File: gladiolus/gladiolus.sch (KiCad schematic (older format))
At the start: 143 parts, among them J1 NEIGHBOR1, J2 NEIGHBOR2, J7 BONUS_ROW, Q1 Q_NPN_BEC, U1 THS4520RGT, U2 AD8330ARQZ, U3 AD9283, U4 AD9704, U5 LMH6643, U6 74LVC1G3157, U7 74LVC1G3157

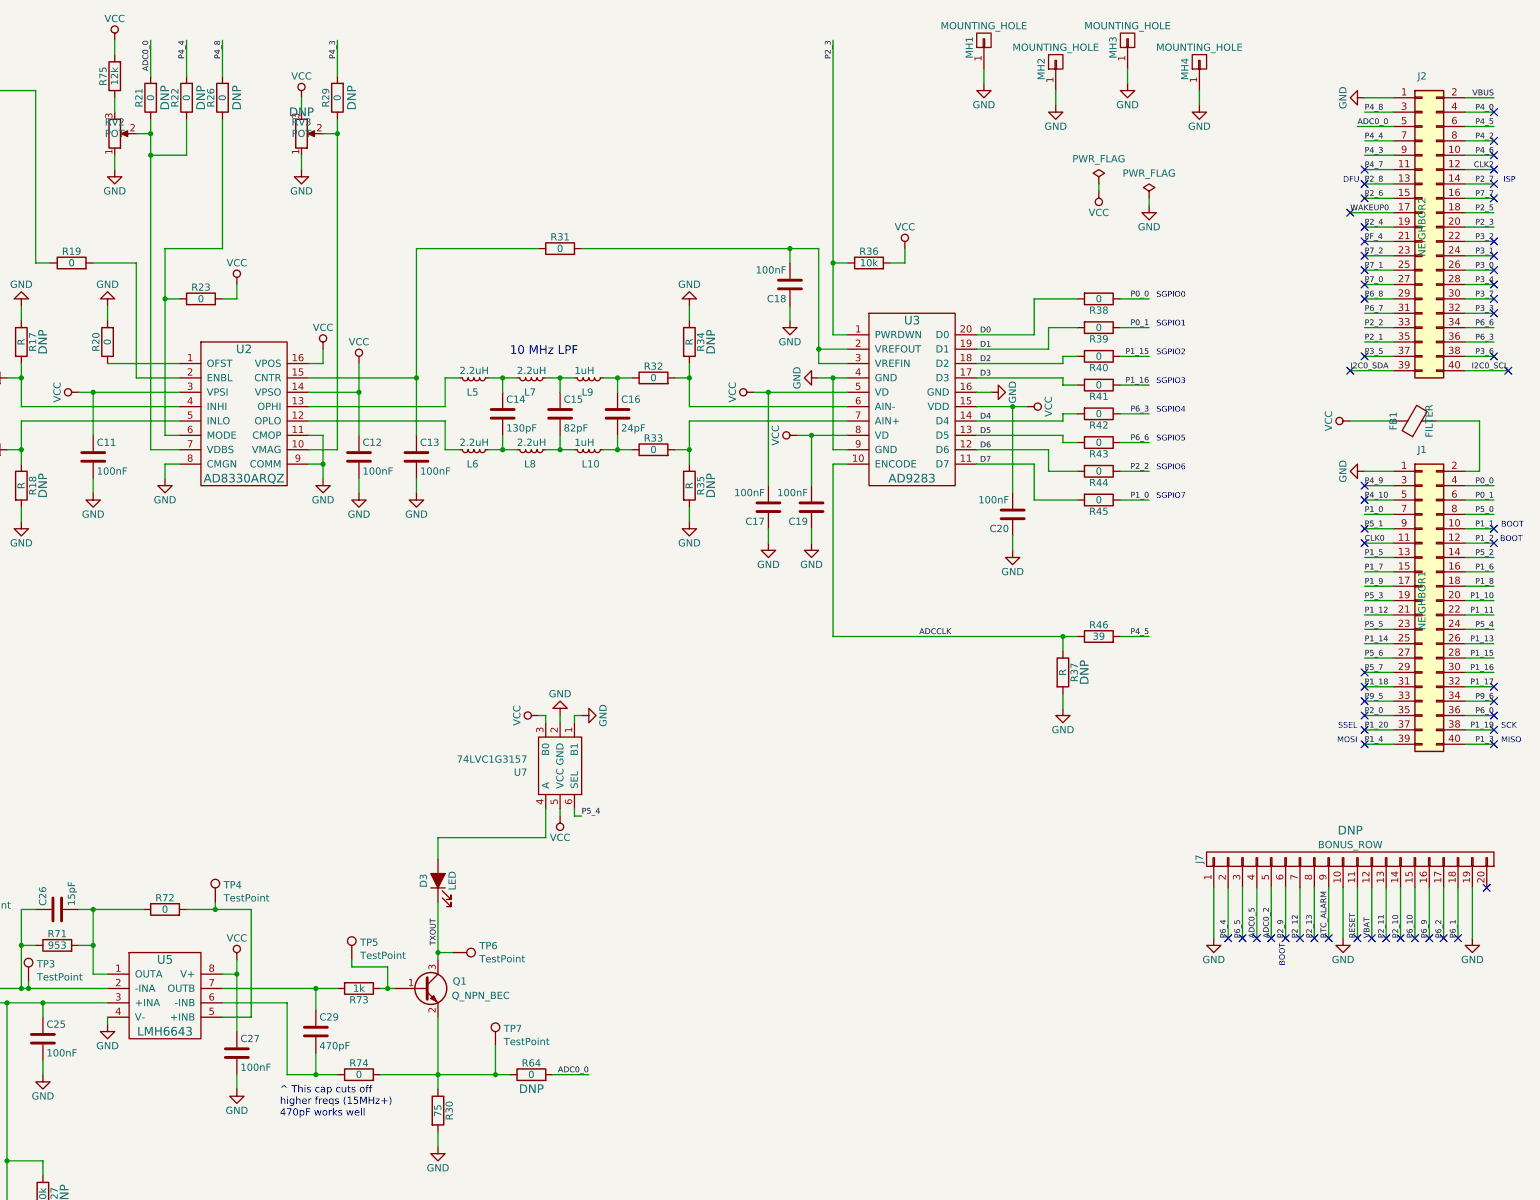
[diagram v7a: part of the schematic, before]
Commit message: Gladiolus: Added EEPROM and changed to default DAC control for second RX gain stage
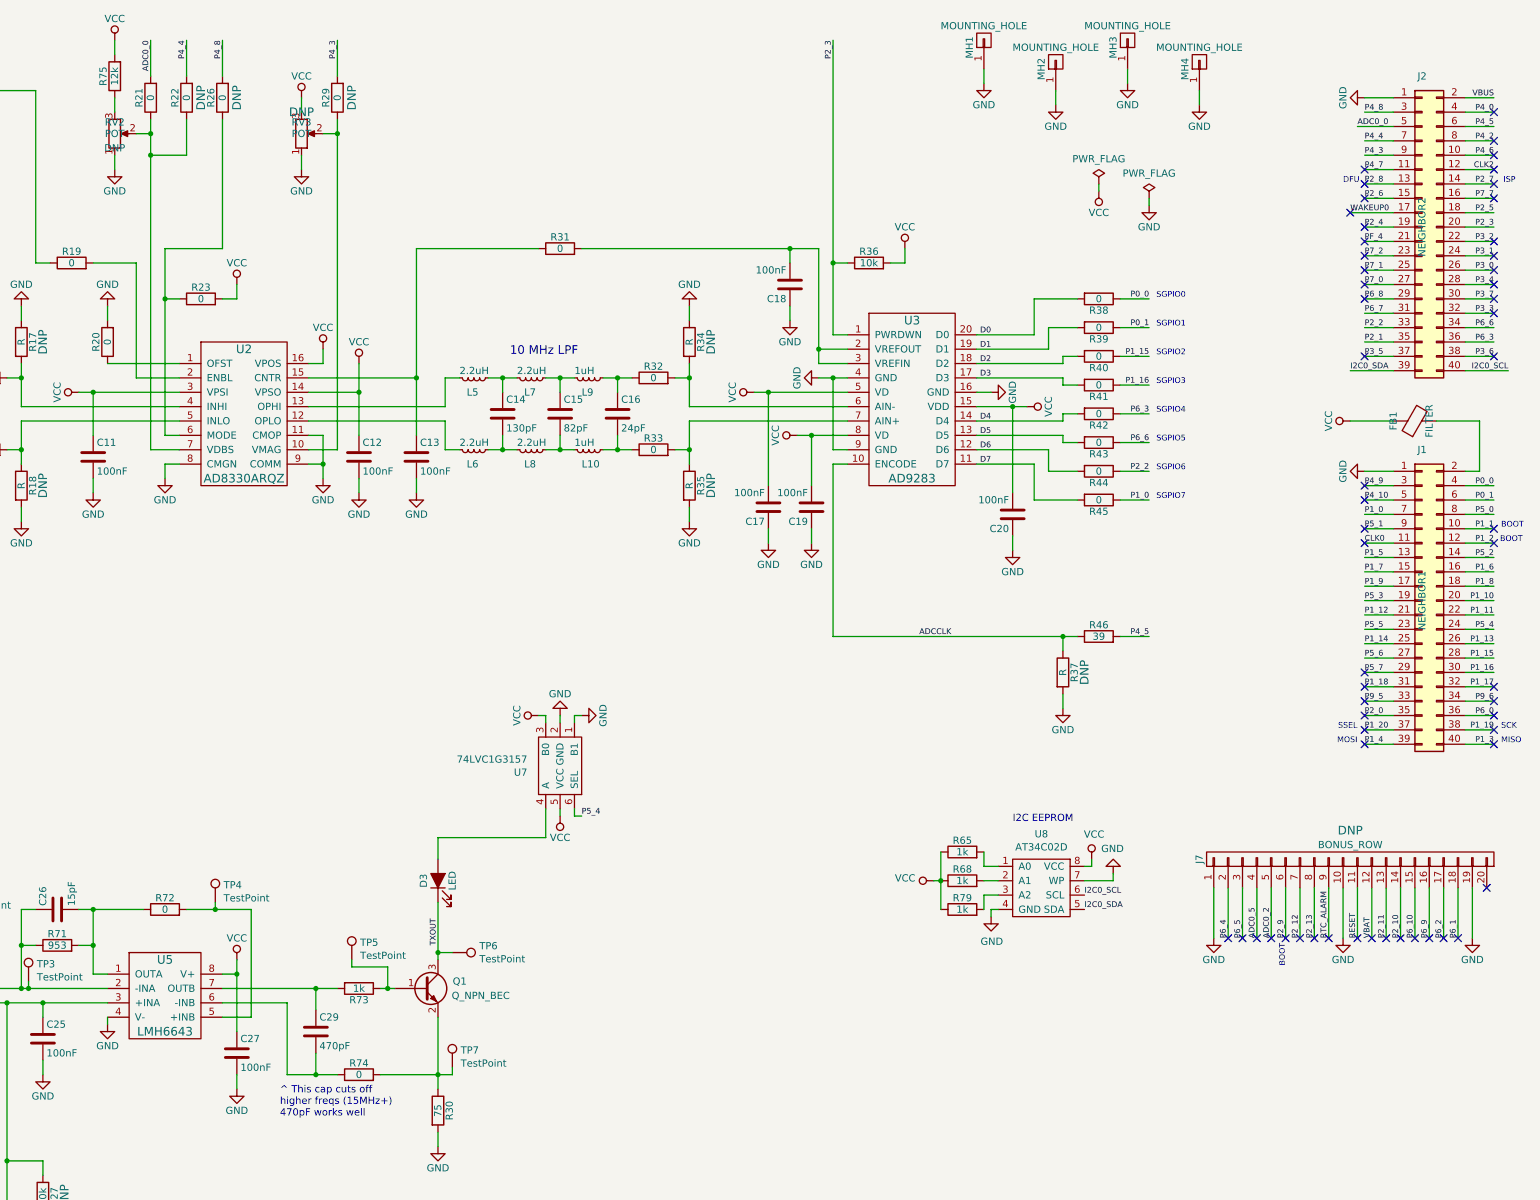
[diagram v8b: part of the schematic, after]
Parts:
- removed R64: 0, gsg-modules:0603, symbol Device:R
- added R65, R68, R79: 1k, gsg-modules:0603, symbol Device:R
- added U8: AT34C02D, gsg-modules:SOIC8-154, symbol gsg-symbols:AT34C02D
- R21: Note DNP -> (none)
- RV2: Note (none) -> DNP
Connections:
- net GND: now also U8.4 (GND), U8.7 (WP)
- net I2C0_SCL: now also U8.6 (SCL)
- net I2C0_SDA: now also U8.5 (SDA)
- net VCC: now also R65.1, R68.1, R79.1, U8.8 (VCC)
- new net: R65.2, U8.1 (A0)
- new net: R68.2, U8.2 (A1)
- new net: R79.2, U8.3 (A2)
- no-connect marks 62 -> 60
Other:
- note added: "I2C EEPROM"
- moved on the sheet: TP7
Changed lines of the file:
@@
 F 5 "RC0603JR-070RL" H 6850 1200 60  0001 C CNN "Part Number"
 F 6 "RES SMD 0.0OHM JUMPER 1/10W 0603" H 6850 1200 60  0001 C CNN "Description"
-F 7 "DNP" V 6750 1200 60  0000 C CNN "Note"
 	1    6850 1200
 	-1   0    0    1
@@
 F 5 "3306F-1-103" H 6600 1450 60  0001 C CNN "Part Number"
 F 6 "10k Ohm 0.2W, 1/5W PC Pins Through Hole Trimmer Potentiometer Cermet 1 Turn Top Adjustment" H 6600 1450 60  0001 C CNN "Description"
+F 7 "DNP" H 6600 1550 50  0000 C CNN "Note"
 	1    6600 1450
 	1    0    0    1
@@
 Wire Wire Line
 	6550 7600 6550 7650
-$Comp
-L Device:R R64
-U 1 1 5CDFA3FF
-P 9500 8000
-F 0 "R64" V 9580 8000 50  0000 C CNN
-F 1 "0" V 9500 8000 50  0000 C CNN
-F 2 "gsg-modules:0603" V 9430 8000 50  0001 C CNN
-F 3 "" H 9500 8000 50  0000 C CNN
-F 4 "Yageo" H 9500 8000 60  0001 C CNN "Manufacturer"
-F 5 "RC0603JR-070RL" H 9500 8000 60  0001 C CNN "Part Number"
-F 6 "RES SMD 0.0OHM JUMPER 1/10W 0603" H 9500 8000 60  0001 C CNN "Description"
-F 7 "DNP" V 9400 8000 60  0000 C CNN "Note"
-	1    9500 8000
-	0    -1   -1   0
-$EndComp
-Text Label 9900 8000 2    40   ~ 0
-ADC0_0
-Wire Wire Line
-	9900 8000 9650 8000
 Wire Wire Line
 	5650 6900 5650 7500
@@
 NoConn ~ 15300 2500
 NoConn ~ 15300 2600
-NoConn ~ 15200 3100
-NoConn ~ 16300 3100
 NoConn ~ 16200 3000
 NoConn ~ 16200 2700
@@
 NoConn ~ 15950 7050
 Wire Wire Line
-	8850 8000 9250 8000
-Connection ~ 9250 8000
-Wire Wire Line
-	9250 8000 9350 8000
-Wire Wire Line
 	8850 6500 8850 6350
 Wire Wire Line
@@
 L Connector:TestPoint TP7
 U 1 1 5CCC58CD
-P 9250 7800
-F 0 "TP7" H 9308 7920 50  0000 L CNN
-F 1 "TestPoint" H 9308 7829 50  0000 L CNN
-F 2 "gsg-modules:TESTPOINT-50MIL" H 9450 7800 50  0001 C CNN
-F 3 "~" H 9450 7800 50  0001 C CNN
-	1    9250 7800
+P 8950 7950
+F 0 "TP7" H 9008 8070 50  0000 L CNN
+F 1 "TestPoint" H 9008 7979 50  0000 L CNN
+F 2 "gsg-modules:TESTPOINT-50MIL" H 9150 7950 50  0001 C CNN
+F 3 "~" H 9150 7950 50  0001 C CNN
+	1    8950 7950
 	1    0    0    -1
 $EndComp
 Wire Wire Line
-	9250 7800 9250 8000
-Wire Wire Line
 	8850 6800 8850 7150
 Wire Wire Line
@@
 NoConn ~ 16200 5300
 NoConn ~ 16200 5400
+$Comp
+L gsg-symbols:AT34C02D U8
+U 1 1 5CD73F24
+P 13050 6700
+F 0 "U8" H 13050 7075 50  0000 C CNN
+F 1 "AT34C02D" H 13050 6984 50  0000 C CNN
+F 2 "gsg-modules:SOIC8-154" H 13100 6650 50  0001 C CNN
+F 3 "" H 13100 6650 50  0001 C CNN
+F 4 "Microchip Technology" H 13050 6700 50  0001 C CNN "Manufacturer"
+F 5 "AT34C02D-SSHM-B" H 13050 6700 50  0001 C CNN "Part Number"
+F 6 "IC EEPROM 2K I2C 1MHZ 8SOIC " H 13050 6700 50  0001 C CNN "Description"
+	1    13050 6700
+	1    0    0    -1
+$EndComp
+Wire Wire Line
+	12750 6850 12700 6850
+Wire Wire Line
+	12700 6850 12700 6900
+$Comp
+L power:GND #PWR059
+U 1 1 5CDD894A
+P 12700 6900
+F 0 "#PWR059" H 12700 6650 50  0001 C CNN
+F 1 "GND" H 12705 6727 50  0000 C CNN
+F 2 "" H 12700 6900 50  0001 C CNN
+F 3 "" H 12700 6900 50  0001 C CNN
+	1    12700 6900
+	1    0    0    -1
+$EndComp
+$Comp
+L power:VCC #PWR075
+U 1 1 5CDD9E7B
+P 13400 6500
+F 0 "#PWR075" H 13400 6350 50  0001 C CNN
+F 1 "VCC" H 13417 6673 50  0000 C CNN
+F 2 "" H 13400 6500 50  0001 C CNN
+F 3 "" H 13400 6500 50  0001 C CNN
+	1    13400 6500
+	1    0    0    -1
+$EndComp
+Wire Wire Line
+	13350 6550 13400 6550
+Wire Wire Line
+	13400 6550 13400 6500
+$Comp
+L power:GND #PWR088
+U 1 1 5CEA0B08
+P 13550 6600
+F 0 "#PWR088" H 13550 6350 50  0001 C CNN
+F 1 "GND" H 13555 6427 50  0000 C CNN
+F 2 "" H 13550 6600 50  0001 C CNN
+F 3 "" H 13550 6600 50  0001 C CNN
+	1    13550 6600
+	-1   0    0    1
+$EndComp
+Wire Wire Line
+	13550 6650 13550 6600
+Wire Wire Line
+	13350 6650 13550 6650
+Text Label 13350 6850 0    40   ~ 0
+I2C0_SDA
+Text Label 13350 6750 0    40   ~ 0
+I2C0_SCL
+$Comp
+L Device:R R68
+U 1 1 5CF0E494
+P 12500 6650
+F 0 "R68" V 12580 6650 50  0000 C CNN
+F 1 "1k" V 12500 6650 50  0000 C CNN
+F 2 "gsg-modules:0603" V 12430 6650 50  0001 C CNN
+F 3 "" H 12500 6650 50  0000 C CNN
+F 4 "Yageo" H 12500 6650 60  0001 C CNN "Manufacturer"
+F 5 "RC0603JR-071KL" H 12500 6650 60  0001 C CNN "Part Number"
+F 6 "RES SMD 1K OHM 5% 1/10W 0603" H 12500 6650 60  0001 C CNN "Description"
+	1    12500 6650
+	0    -1   -1   0
+$EndComp
+$Comp
+L Device:R R65
+U 1 1 5CF0ED14
+P 12500 6450
+F 0 "R65" V 12580 6450 50  0000 C CNN
+F 1 "1k" V 12500 6450 50  0000 C CNN
+F 2 "gsg-modules:0603" V 12430 6450 50  0001 C CNN
+F 3 "" H 12500 6450 50  0000 C CNN
+F 4 "Yageo" H 12500 6450 60  0001 C CNN "Manufacturer"
+F 5 "RC0603JR-071KL" H 12500 6450 60  0001 C CNN "Part Number"
+F 6 "RES SMD 1K OHM 5% 1/10W 0603" H 12500 6450 60  0001 C CNN "Description"
+	1    12500 6450
+	0    -1   -1   0
+$EndComp
+$Comp
+L Device:R R79
+U 1 1 5CF0F29C
+P 12500 6850
+F 0 "R79" V 12580 6850 50  0000 C CNN
+F 1 "1k" V 12500 6850 50  0000 C CNN
+F 2 "gsg-modules:0603" V 12430 6850 50  0001 C CNN
+F 3 "" H 12500 6850 50  0000 C CNN
+F 4 "Yageo" H 12500 6850 60  0001 C CNN "Manufacturer"
+F 5 "RC0603JR-071KL" H 12500 6850 60  0001 C CNN "Part Number"
+F 6 "RES SMD 1K OHM 5% 1/10W 0603" H 12500 6850 60  0001 C CNN "Description"
+	1    12500 6850
+	0    -1   -1   0
+$EndComp
+Wire Wire Line
+	12750 6750 12650 6750
+Wire Wire Line
+	12650 6750 12650 6850
+Wire Wire Line
+	12650 6550 12650 6450
+Wire Wire Line
+	12650 6550 12750 6550
+Wire Wire Line
+	12650 6650 12750 6650
+$Comp
+L power:VCC #PWR046
+U 1 1 5D1097BE
+P 12300 6650
+F 0 "#PWR046" H 12300 6500 50  0001 C CNN
+F 1 "VCC" V 12318 6777 50  0000 L CNN
+F 2 "" H 12300 6650 50  0001 C CNN
+F 3 "" H 12300 6650 50  0001 C CNN
+	1    12300 6650
+	0    -1   -1   0
+$EndComp
+Wire Wire Line
+	12300 6650 12350 6650
+Wire Wire Line
+	12350 6650 12350 6450
+Connection ~ 12350 6650
+Wire Wire Line
+	12350 6650 12350 6850
+Text Notes 12850 6250 0    50   ~ 0
+I2C EEPROM
+Wire Wire Line
+	8850 8000 8950 8000
+Wire Wire Line
+	8950 8000 8950 7950
 $EndSCHEMATC
